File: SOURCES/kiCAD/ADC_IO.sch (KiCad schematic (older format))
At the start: 161 parts, among them IC2 PCM1808QPWRQ1, J1 Conn_01x08, J10 Conn_01x02, J11 Conn_Coaxial, J12 IDC_2x5, J3 Conn_01x08, J5 MJ-519, J6 8P_DIP_SOCKET, J9 Conn_01x02, Q12 MJD45H11T4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

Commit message: Released for everyone, ready to build.
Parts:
- added C168: 10uF, Capacitor_SMD:C_0805_2012Metric_Pad1.18x1.45mm_HandSolder, symbol Device:C_Small
- C25, C26, C29, C30: Description (none) -> C0G or ECHU(FilmCap) Recommended
- C27, C28: Description Audio Grade Cap Recommended -> Audio Grade Ele-Cap or WIMA Recommended
- D21: Description (none) -> Si Switching Diode
- D24: Description (none) -> SBDfor Level Clampling
- D25: Description (none) -> SBD for Level Clampling
- FB1: Description FERRITE BEAD 330 OHM 0805 1LN -> Bead for connecting AnalogGND and DigitalGND
- FB3: Description FERRITE BEAD 600 OHM -> Bead for PLL Power Rail
- FB4: Description FERRITE BEAD 600 OHM -> Bead for Analog Core
- J12: Description 10pin IDC header for USBi -> Angled 10pin IDC header for USBi
- J5: value MJ-519 -> RCJ-2223; footprint MyJacks:MJ-519 -> MyJacks:RCJ-2223; Description Vertical Stereo RCA-pin Jack (Upper=Left, Lower=Right) RCJ-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 -> Vertical Stereo RCA-pin Jack (Upper=Right, Lower=Left) RCJ-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
- J6: Description Just Prepared for the Altanative choice of EEPROM package -> Optional Sockt for substitute package of SPI-EEPROM
- Q12: Description (none) -> PNP Transistor for 1.2V Power Rail
- Q13, Q30, Q31: Description (none) -> N-CHANNEL ENHANCEMENT MODE MOSFET
- R38: Description (none) -> Prepared for Damping Control
- R43: Description (none) -> Remove this when Using SW4
- R74: value 4.7k -> 100k; JLPCB# C23162 -> C25803
- R76: value 560R -> 1.2k; JLPCB# C23204 -> C22765
- RV1, RV2, RV3, RV4, RV5: Description (none) -> Potentiometer for AUX Voltage Control
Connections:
- net GND: now also C168.1
- net ~DSP-RESET: now also C168.2
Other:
- moved on the sheet: C25, C26, C27, C28, J5, Q13, R24, R25, R85, R86

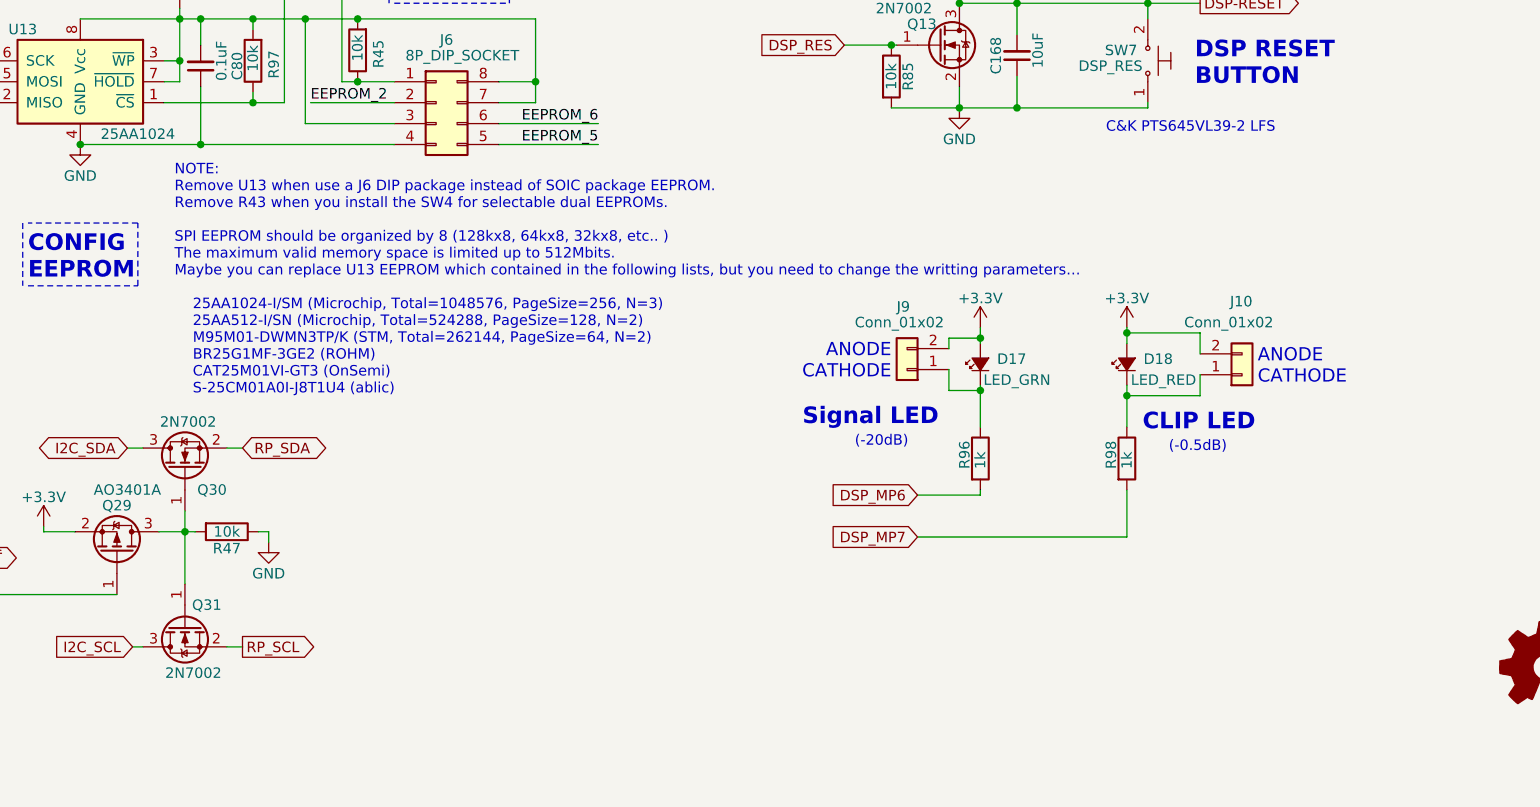
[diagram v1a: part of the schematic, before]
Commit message: Fixed ACM9070 lands. Selectable I2C for RPI/YORK
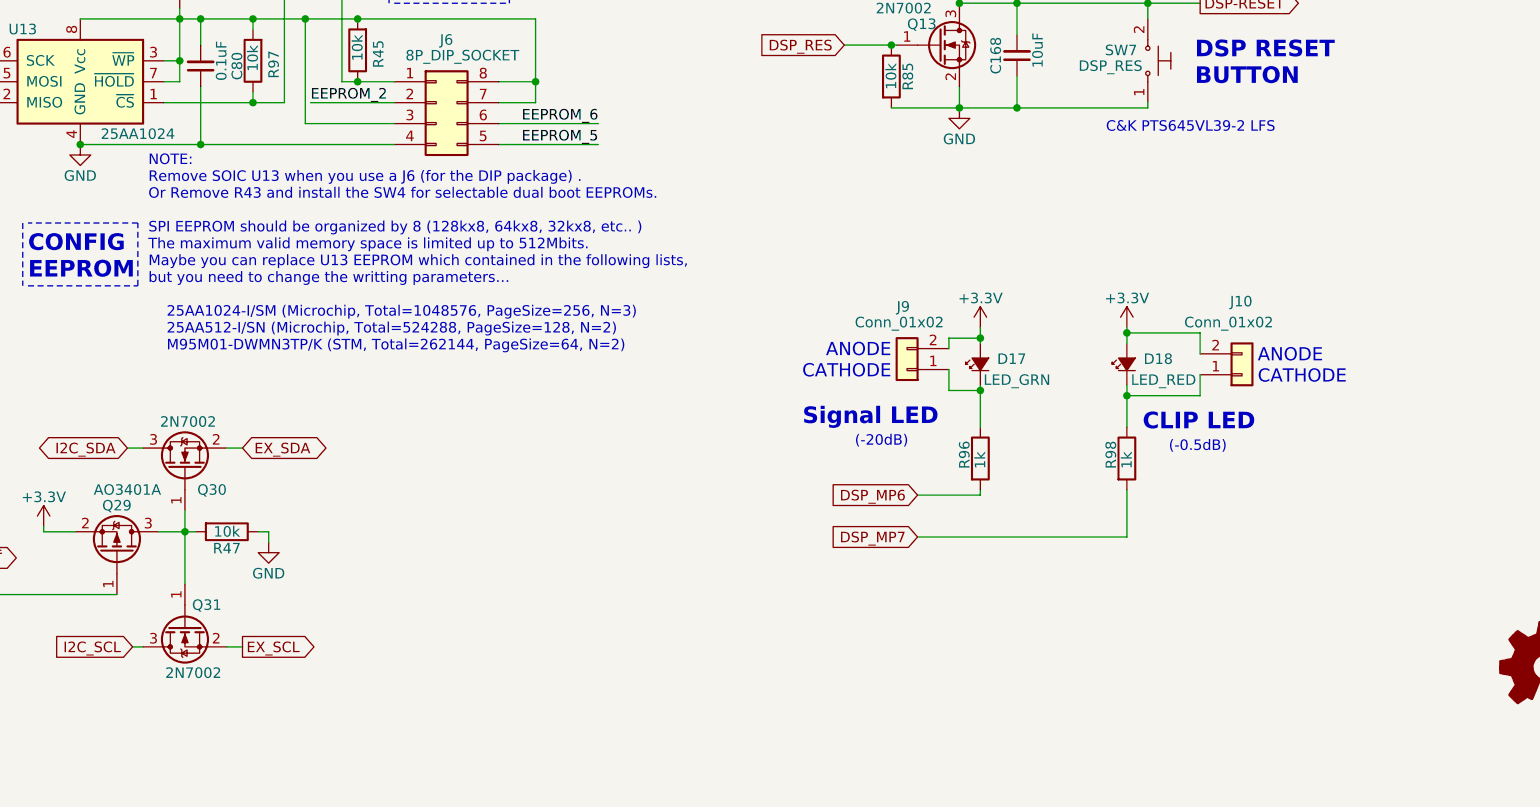
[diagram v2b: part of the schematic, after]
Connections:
- net RP_SCL renamed EX_SCL
- net RP_SDA renamed EX_SDA
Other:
- note added: "NOTE:\nRemove SOIC U13 when you use a J6 (for the DIP package) .\nOr Remove R43 and install the SW4 for selectable dual boot EEPROMs.\n\nSPI EEPROM should be organized by 8 (128kx8, 64kx8, 32kx8, etc.. )\nThe maximum valid memory space is limited up to 512Mbits.\nMaybe you can replace U13 EEPROM which contained in the following lists, \nbut you need to change the writting parameters…\n\n 25AA1024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"
- note removed: "NOTE:\nRemove U13 when use a J6 DIP package instead of SOIC package EEPROM.\nRemove R43 when you install the SW4 for selectable dual EEPROMs.\n\nSPI EEPROM should be organized by 8 (128kx8, 64kx8, 32kx8, etc.. )\nThe maximum valid memory space is limited up to 512Mbits.\nMaybe you can replace U13 EEPROM which contained in the following lists, but you need to change the writting parameters…\n\n 25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"
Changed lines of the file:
@@
 Title "FreeDSP OCTAVIA ADC/DSP Part"
 Date "2023-09-30"
-Rev "1.00"
+Rev "1.1"
 Comp ""
 Comment1 ""
@@
 	6600 9450 6675 9450
 Text GLabel 9425 9250 2    50   BiDi ~ 0
-RP_SDA
+EX_SDA
 Text GLabel 9425 10200 2    50   Output ~ 0
-RP_SCL
+EX_SCL
 Text GLabel 8900 10200 0    50   Input ~ 0
 I2C_SCL
@@
 Wire Wire Line
 	13650 8950 13650 9000
-Text Notes 9100 9000 0    50   ~ 0
-NOTE:\nRemove U13 when use a J6 DIP package instead of SOIC package EEPROM.\nRemove R43 when you install the SW4 for selectable dual EEPROMs.\n\nSPI EEPROM should be organized by 8 (128kx8, 64kx8, 32kx8, etc.. )\nThe maximum valid memory space is limited up to 512Mbits.\nMaybe you can replace U13 EEPROM which contained in the following lists, but you need to change the writting parameters…\n\n    25AA1024-I/SM (Microchip, Total=1048576, PageSize=256, N=3)\n    25AA512-I/SN (Microchip, Total=524288, PageSize=128, N=2)\n    M95M01-DWMN3TP/K (STM, Total=262144, PageSize=64, N=2)\n    BR25G1MF-3GE2 (ROHM)\n    CAT25M01VI-GT3 (OnSemi)\n    S-25CM01A0I-J8T1U4 (ablic)\n
+Text Notes 8975 8875 0    50   ~ 0
+NOTE:\nRemove SOIC U13 when you use a J6 (for the DIP package) .\nOr Remove R43 and install the SW4 for selectable dual boot EEPROMs.\n\nSPI EEPROM should be organized by 8 (128kx8, 64kx8, 32kx8, etc.. )\nThe maximum valid memory space is limited up to 512Mbits.\nMaybe you can replace U13 EEPROM which contained in the following lists, \nbut you need to change the writting parameters…\n\n    25AA1024-I/SM (Microchip, Total=1048576, PageSize=256, N=3)\n    25AA512-I/SN (Microchip, Total=524288, PageSize=128, N=2)\n    M95M01-DWMN3TP/K (STM, Total=262144, PageSize=64, N=2)\n\n
 $Comp
 L Connector_Generic:Conn_01x02 J10

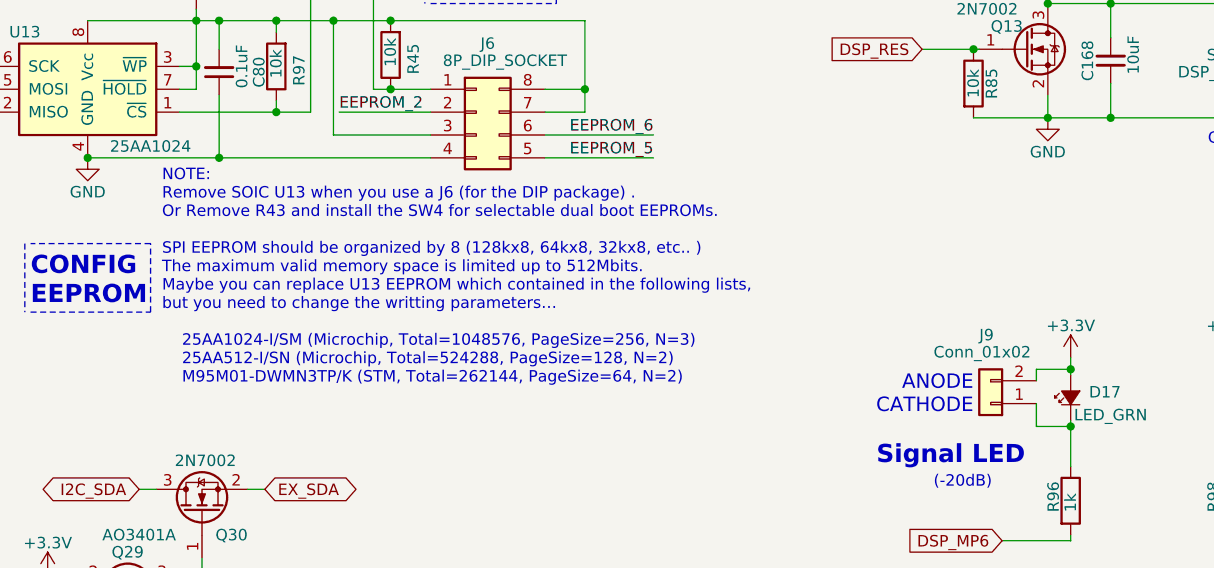
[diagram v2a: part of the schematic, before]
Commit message: A method of board type convertion had changed.
Add an AGND fill on the bottom layer. The connection path for the Standard type board had changed. No features/functions changed.
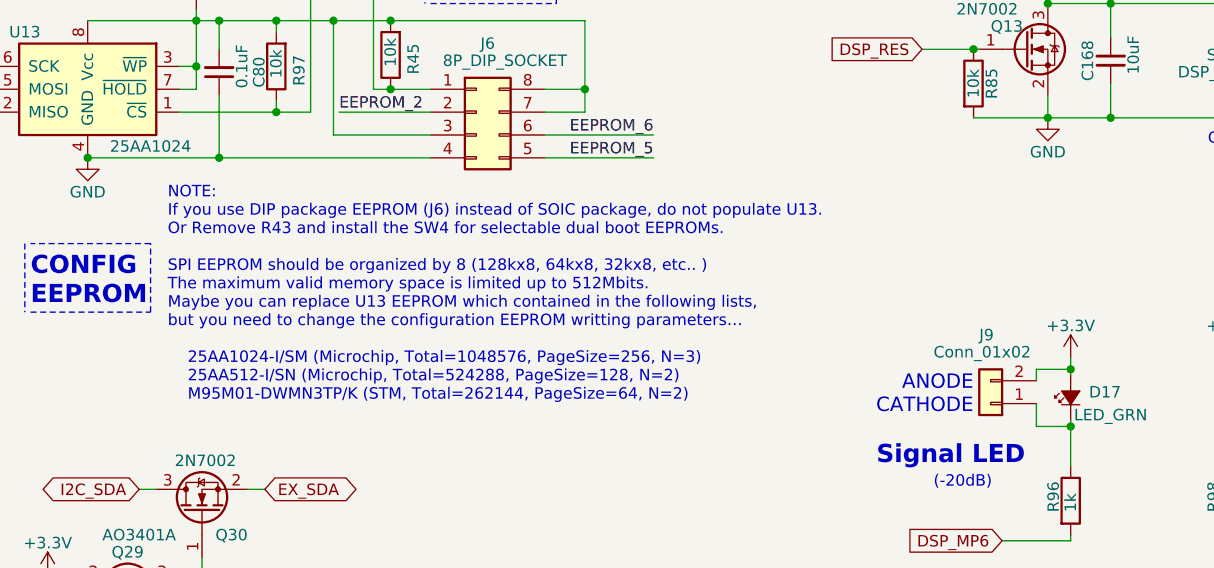
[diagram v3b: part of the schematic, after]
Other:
- note added: "NOTE:\nIf you use DIP package EEPROM (J6) instead of SOIC package, do not populate U13.\nOr Remove R43 and install the SW4 for selectable dual boot EEPROMs.\n\nSPI EEPROM should be organized by 8 (128kx8, 64kx8, 32kx8, etc.. )\nThe maximum valid memory space is limited up to 512Mbits.\nMaybe you can replace U13 EEPROM which contained in the following lists, \nbut you need to change the configurat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"
- note removed: "NOTE:\nRemove SOIC U13 when you use a J6 (for the DIP package) .\nOr Remove R43 and install the SW4 for selectable dual boot EEPROMs.\n\nSPI EEPROM should be organized by 8 (128kx8, 64kx8, 32kx8, etc.. )\nThe maximum valid memory space is limited up to 512Mbits.\nMaybe you can replace U13 EEPROM which contained in the following lists, \nbut you need to change the writting parameters…\n\n 25AA1024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"
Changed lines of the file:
@@
 Sheet 2 3
 Title "FreeDSP OCTAVIA ADC/DSP Part"
-Date "2023-09-30"
-Rev "1.1"
+Date "2024-01-01"
+Rev "1.2"
 Comp ""
 Comment1 ""
@@
 Wire Wire Line
 	13650 8950 13650 9000
-Text Notes 8975 8875 0    50   ~ 0
-NOTE:\nRemove SOIC U13 when you use a J6 (for the DIP package) .\nOr Remove R43 and install the SW4 for selectable dual boot EEPROMs.\n\nSPI EEPROM should be organized by 8 (128kx8, 64kx8, 32kx8, etc.. )\nThe maximum valid memory space is limited up to 512Mbits.\nMaybe you can replace U13 EEPROM which contained in the following lists, \nbut you need to change the writting parameters…\n\n    25AA1024-I/SM (Microchip, Total=1048576, PageSize=256, N=3)\n    25AA512-I/SN (Microchip, Total=524288, PageSize=128, N=2)\n    M95M01-DWMN3TP/K (STM, Total=262144, PageSize=64, N=2)\n\n
+Text Notes 9000 8950 0    50   ~ 0
+NOTE:\nIf you use DIP package EEPROM (J6) instead of SOIC package, do not populate U13.\nOr Remove R43 and install the SW4 for selectable dual boot EEPROMs.\n\nSPI EEPROM should be organized by 8 (128kx8, 64kx8, 32kx8, etc.. )\nThe maximum valid memory space is limited up to 512Mbits.\nMaybe you can replace U13 EEPROM which contained in the following lists, \nbut you need to change the configuration EEPROM writting parameters…\n\n    25AA1024-I/SM (Microchip, Total=1048576, PageSize=256, N=3)\n    25AA512-I/SN (Microchip, Total=524288, PageSize=128, N=2)\n    M95M01-DWMN3TP/K (STM, Total=262144, PageSize=64, N=2)\n\n
 $Comp
 L Connector_Generic:Conn_01x02 J10
